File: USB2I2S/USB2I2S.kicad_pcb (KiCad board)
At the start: 2 copper layers, 27.9 x 38.1 mm, 12 parts, among them J1 Conn_01x08_Male, J2 Conn_01x04_Male, J3 Conn_01x02_Male, J5 Conn_01x01_Male, J8 USB_B_Micro, J9 Conn_01x06_Male, U6 CP2615-A01-GM

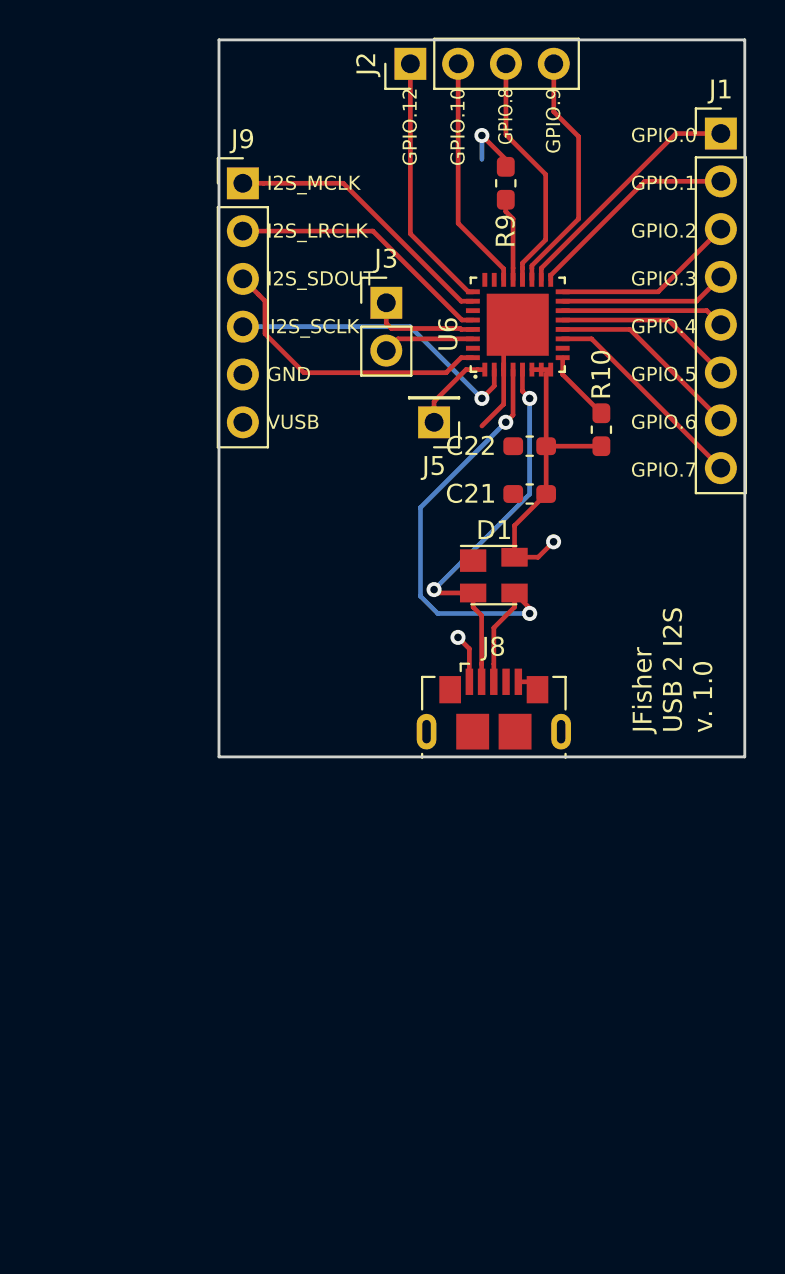
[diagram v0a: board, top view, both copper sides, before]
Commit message: Update USB2I2S board to fix routing issue
- Fixed issue where VCC was connected to VUSB
- Converted PCB to 4-layer board with Vcc and GND planes
- Removed headers for pins that I'm not expecting to use
- Re-layed out the PCB.
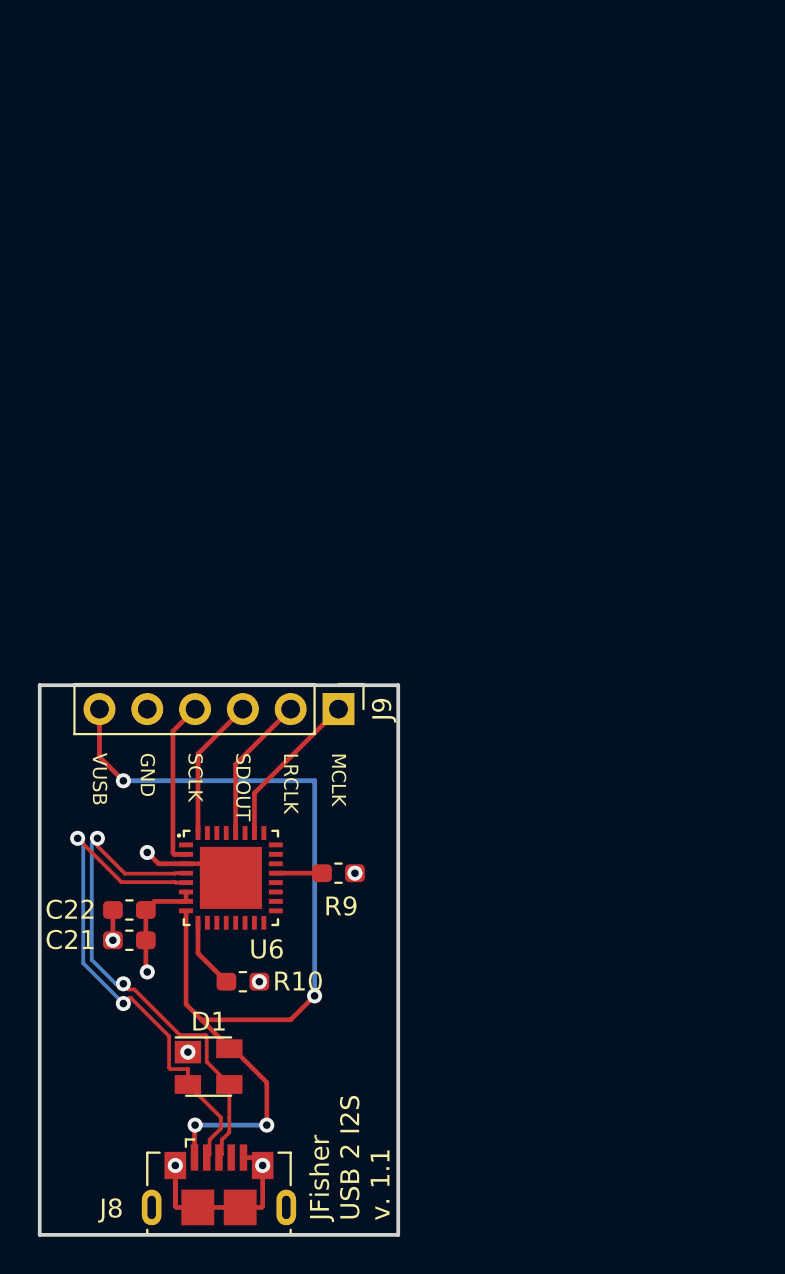
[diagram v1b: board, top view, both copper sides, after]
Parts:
- removed J1: Conn_01x08_Male, Connector_PinHeader_2.54mm:PinHeader_1x08_P2.54mm_Vertical
- removed J2: Conn_01x04_Male, Connector_PinHeader_2.54mm:PinHeader_1x04_P2.54mm_Vertical
- removed J3: Conn_01x02_Male, Connector_PinHeader_2.54mm:PinHeader_1x02_P2.54mm_Vertical
- removed J5: Conn_01x01_Male, Connector_PinHeader_2.54mm:PinHeader_1x01_P2.54mm_Vertical
- moved R9 37.7 mm to (119.4, 121.8), turned to 180 degrees
- moved R10 35.0 mm to (114.3, 127.5), turned to 180 degrees
- moved U6 33.1 mm to (113.7, 122.0), turned to 0 degrees
- moved C22 32.6 mm to (108.3, 123.7)
- moved C21 31.9 mm to (108.3, 125.3)
- moved D1 30.2 mm to (112.5, 132.0)
- moved J8 29.2 mm to (113.0, 138.3)
- moved J9 28.4 mm to (119.4, 113.0), turned to 270 degrees
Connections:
- net VBUS_DN renamed USB_DN
- net VBUS_DP renamed USB_DP
- C21 pad 1: VBUS_IN -> VCC
- C22 pad 1: VBUS_IN -> VCC
- R10 pad 1: VBUS_IN -> VCC
- R9 pad 1: VBUS_IN -> VCC
- U6 pad 1: Net-(J5-Pad1) -> (no net)
- U6 pad 11: Net-(J1-Pad8) -> (no net)
- U6 pad 12: Net-(J1-Pad7) -> (no net)
- U6 pad 13: Net-(J1-Pad6) -> (no net)
- U6 pad 14: Net-(J1-Pad5) -> (no net)
- U6 pad 15: Net-(J1-Pad4) -> (no net)
- U6 pad 16: Net-(J1-Pad3) -> (no net)
- U6 pad 17: Net-(J1-Pad2) -> (no net)
- U6 pad 18: Net-(J1-Pad1) -> (no net)
- U6 pad 19: Net-(J2-Pad4) -> (no net)
- U6 pad 20: Net-(J2-Pad3) -> (no net)
- U6 pad 22: Net-(J2-Pad2) -> (no net)
- U6 pad 25: Net-(J2-Pad1) -> (no net)
- U6 pad 29: Net-(J3-Pad1) -> (no net)
- U6 pad 30: Net-(J3-Pad2) -> (no net)
- U6 pad 6: VBUS_IN -> VCC
- U6 pad 7: VBUS_IN -> VCC
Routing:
- net VBUS_IN: track 23.2 -> 51.3 mm, vias 3 -> 4
- net Net-(J2-Pad1): track 13.6 -> 0.00 mm
- net Net-(J1-Pad1): track 13.1 -> 0.00 mm
- net Net-(J2-Pad4): track 13.1 -> 0.00 mm
- net Net-(J2-Pad3): track 12.9 -> 0.00 mm
- net Net-(J2-Pad2): track 12.5 -> 0.00 mm
- net GND: track 7.36 -> 19.0 mm, vias 0 -> 5
- net Net-(J1-Pad2): track 11.4 -> 0.00 mm
- net Net-(J1-Pad8): track 11.3 -> 0.00 mm
- net Net-(J1-Pad7): track 10.4 -> 0.00 mm
- net Net-(J1-Pad3): track 9.79 -> 0.00 mm
- net Net-(J1-Pad6): track 9.56 -> 0.00 mm
- net Net-(J1-Pad4): track 8.94 -> 0.00 mm
- net Net-(J1-Pad5): track 8.72 -> 0.00 mm
- net I2S_SDOUT: track 15.6 -> 7.57 mm
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- added copper zone on In1.Cu, net GND
- added copper zone on In2.Cu, net VCC
- removed copper zone on F.Cu, net GND
- removed copper zone on B.Cu, net VBUS_IN
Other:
- board size 27.9 x 38.1 mm -> 19.1 x 29.2 mm
- copper layers 2 -> 4
- board text added: "JFisher USB 2 I2S v. 1.1"
- board text added: "LRCLK"
- board text added: "MCLK"
- board text added: "SCLK"
- board text added: "SDOUT"
- board text removed: "GPIO.0"
- board text removed: "GPIO.1"
- board text removed: "GPIO.10"
- board text removed: "GPIO.12"
- board text removed: "GPIO.2"
- board text removed: "GPIO.3"
- board text removed: "GPIO.4"
- board text removed: "GPIO.5"
- board text removed: "GPIO.6"
- board text removed: "GPIO.7"
- board text removed: "GPIO.8"
- board text removed: "GPIO.9"
- board text removed: "I2S_LRCLK"
- board text removed: "I2S_MCLK"
- board text removed: "I2S_SCLK"
- board text removed: "I2S_SDOUT"
- board text removed: "JFisher USB 2 I2S v. 1.0"

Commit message: Update KiCad and minor adjustments (cosmetic)
Rotated the decoupling caps on Vcc to ensure that the blind vias were
away from the differential USB signal traces.
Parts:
- moved C21 1.77 mm to (109.6, 124.1), turned to 270 degrees
- moved C22 0.54 mm to (108.0, 124.1), turned to 270 degrees
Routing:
- net VCC: track 6.15 -> 3.84 mm, vias 3 -> 4
- net GND: vias 5 -> 6
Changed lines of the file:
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@@
-(kicad_pcb (version 20171130) (host pcbnew "(5.0.2)-1")
+(kicad_pcb (version 20171130) (host pcbnew "(5.1.0)-1")
   (general
     (thickness 1.6)
     (drawings 11)
-    (tracks 108)
+    (tracks 110)
     (zones 0)
     (modules 8)
@@
     (0 F.Cu signal)
     (1 In1.Cu signal)
-    (2 In2.Cu signal hide)
+    (2 In2.Cu signal)
     (31 B.Cu signal)
     (33 F.Adhes user)
@@
     (zone_45_only no)
     (trace_min 0.2)
-    (segment_width 0.2)
-    (edge_width 0.15)
     (via_size 0.8)
     (via_drill 0.4)
@@
     (uvia_min_size 0.2)
     (uvia_min_drill 0.1)
+    (edge_width 0.15)
+    (segment_width 0.2)
     (pcb_text_width 0.3)
     (pcb_text_size 1.5 1.5)
@@
   )
   (module Capacitor_SMD:C_0603_1608Metric_Pad1.05x0.95mm_HandSolder (layer F.Cu)
-    (at 108.268472 125.313627 180)
+    (at 109.601 124.141528 270)
     (descr "Capacitor SMD 0603 (1608 Metric), square (rectangular) end terminal, IPC_7351 nominal with elongated pad for handsoldering. (Body size source: http://www.tortai-tech.com/upload/download/2011102023233369053.pdf), generated with kicad-footprint-generator")
     (tags "capacitor handsolder")
     (attr smd)
-    (fp_text reference C21 (at 3.124999 0 180) (layer F.SilkS)
-      (effects (font (size 1 1) (thickness 0.15)))
-    )
-    (fp_text value 1uF (at 0 0 180) (layer F.Fab)
-      (effects (font (size 1 1) (thickness 0.15)))
-    )
-    (fp_text user %R (at 0 0 180) (layer F.Fab)
+    (fp_text reference C21 (at 3.124999 0 270) (layer F.SilkS)
+      (effects (font (size 1 1) (thickness 0.15)))
+    )
+    (fp_text value 1uF (at 0 0 270) (layer F.Fab)
+      (effects (font (size 1 1) (thickness 0.15)))
+    )
+    (fp_text user %R (at 0 0 270) (layer F.Fab)
       (effects (font (size 0.4 0.4) (thickness 0.06)))
     )
@@
     (fp_line (start -0.8 -0.4) (end 0.8 -0.4) (layer F.Fab) (width 0.1))
     (fp_line (start -0.8 0.4) (end -0.8 -0.4) (layer F.Fab) (width 0.1))
-    (pad 2 smd roundrect (at 0.875 0 180) (size 1.05 0.95) (layers F.Cu F.Paste F.Mask) (roundrect_rratio 0.25)
-      (net 1 GND))
-    (pad 1 smd roundrect (at -0.875 0 180) (size 1.05 0.95) (layers F.Cu F.Paste F.Mask) (roundrect_rratio 0.25)
+    (pad 2 smd roundrect (at 0.875 0 270) (size 1.05 0.95) (layers F.Cu F.Paste F.Mask) (roundrect_rratio 0.25)
+      (net 1 GND))
+    (pad 1 smd roundrect (at -0.875 0 270) (size 1.05 0.95) (layers F.Cu F.Paste F.Mask) (roundrect_rratio 0.25)
       (net 9 VCC))
     (model ${KISYS3DMOD}/Capacitor_SMD.3dshapes/C_0603_1608Metric.wrl
@@
   )
   (module Capacitor_SMD:C_0603_1608Metric_Pad1.05x0.95mm_HandSolder (layer F.Cu)
-    (at 108.268472 123.7065 180)
+    (at 107.95 124.141528 270)
     (descr "Capacitor SMD 0603 (1608 Metric), square (rectangular) end terminal, IPC_7351 nominal with elongated pad for handsoldering. (Body size source: http://www.tortai-tech.com/upload/download/2011102023233369053.pdf), generated with kicad-footprint-generator")
     (tags "capacitor handsolder")
     (attr smd)
-    (fp_text reference C22 (at 3.124999 0 180) (layer F.SilkS)
-      (effects (font (size 1 1) (thickness 0.15)))
-    )
-    (fp_text value 0.1uF (at 0 0 180) (layer F.Fab)
+    (fp_text reference C22 (at 3.124999 0 270) (layer F.SilkS)
+      (effects (font (size 1 1) (thickness 0.15)))
+    )
+    (fp_text value 0.1uF (at 0 0 270) (layer F.Fab)
       (effects (font (size 1 1) (thickness 0.15)))
     )
@@
     (fp_line (start 1.65 -0.73) (end 1.65 0.73) (layer F.CrtYd) (width 0.05))
     (fp_line (start 1.65 0.73) (end -1.65 0.73) (layer F.CrtYd) (width 0.05))
-    (fp_text user %R (at 0 0 180) (layer F.Fab)
+    (fp_text user %R (at 0 0 270) (layer F.Fab)
       (effects (font (size 0.4 0.4) (thickness 0.06)))
     )
-    (pad 1 smd roundrect (at -0.875 0 180) (size 1.05 0.95) (layers F.Cu F.Paste F.Mask) (roundrect_rratio 0.25)
+    (pad 1 smd roundrect (at -0.875 0 270) (size 1.05 0.95) (layers F.Cu F.Paste F.Mask) (roundrect_rratio 0.25)
       (net 9 VCC))
-    (pad 2 smd roundrect (at 0.875 0 180) (size 1.05 0.95) (layers F.Cu F.Paste F.Mask) (roundrect_rratio 0.25)
+    (pad 2 smd roundrect (at 0.875 0 270) (size 1.05 0.95) (layers F.Cu F.Paste F.Mask) (roundrect_rratio 0.25)
       (net 1 GND))
     (model ${KISYS3DMOD}/Capacitor_SMD.3dshapes/C_0603_1608Metric.wrl
@@
   (segment (start 111.28 121.25) (end 109.82 121.25) (width 0.25) (layer F.Cu) (net 1))
   (segment (start 109.82 121.25) (end 109.22 120.65) (width 0.25) (layer F.Cu) (net 1))
-  (segment (start 107.393472 123.7065) (end 107.393472 125.313627) (width 0.25) (layer F.Cu) (net 1))
-  (via (at 107.393472 125.313627) (size 0.8) (drill 0.4) (layers F.Cu B.Cu) (net 1))
-  (via (at 111.379 131.2575) (size 0.8) (drill 0.4) (layers F.Cu B.Cu) (net 1))
+  (via blind (at 111.379 131.2575) (size 0.8) (drill 0.4) (layers F.Cu In1.Cu) (net 1))
   (segment (start 114.93 136.8615) (end 115.35 137.2815) (width 0.25) (layer F.Cu) (net 1))
   (segment (start 114.33 136.8615) (end 114.93 136.8615) (width 0.25) (layer F.Cu) (net 1))
@@
   (segment (start 110.78 139.5115) (end 110.71 139.4415) (width 0.25) (layer F.Cu) (net 1))
   (segment (start 111.905 139.5115) (end 110.78 139.5115) (width 0.25) (layer F.Cu) (net 1))
-  (via (at 110.71 137.2815) (size 0.8) (drill 0.4) (layers F.Cu B.Cu) (net 1))
+  (via blind (at 110.71 137.2815) (size 0.8) (drill 0.4) (layers F.Cu In1.Cu) (net 1))
   (segment (start 110.71 137.2815) (end 110.71 139.4415) (width 0.25) (layer F.Cu) (net 1))
-  (via (at 115.35 137.2815) (size 0.8) (drill 0.4) (layers F.Cu B.Cu) (net 1))
+  (via blind (at 115.35 137.2815) (size 0.8) (drill 0.4) (layers F.Cu In1.Cu) (net 1))
+  (segment (start 109.601 125.016528) (end 109.601 125.016528) (width 0.25) (layer F.Cu) (net 1))
+  (segment (start 107.95 125.016528) (end 107.95 125.016528) (width 0.25) (layer F.Cu) (net 1))
+  (via blind (at 107.95 125.016528) (size 0.8) (drill 0.4) (layers F.Cu In1.Cu) (net 1))
+  (segment (start 109.601 125.016528) (end 107.95 125.016528) (width 0.25) (layer F.Cu) (net 1))
+  (via blind (at 109.601 125.016528) (size 0.8) (drill 0.4) (layers F.Cu In1.Cu) (net 1))
   (segment (start 111.73 136.8615) (end 111.73 135.1665) (width 0.25) (layer F.Cu) (net 2))
   (segment (start 111.73 135.1665) (end 111.76 135.1365) (width 0.25) (layer F.Cu) (net 2))
@@
   (segment (start 113.425 127.5165) (end 111.915 126.0065) (width 0.25) (layer F.Cu) (net 8))
   (via blind (at 120.255 121.75) (size 0.8) (drill 0.4) (layers F.Cu In2.Cu) (net 9))
-  (segment (start 109.143472 125.313627) (end 109.143472 123.7065) (width 0.25) (layer F.Cu) (net 9))
-  (segment (start 109.599972 123.25) (end 111.28 123.25) (width 0.25) (layer F.Cu) (net 9))
-  (segment (start 109.143472 123.7065) (end 109.599972 123.25) (width 0.25) (layer F.Cu) (net 9))
   (segment (start 111.28 122.75) (end 111.28 123.25) (width 0.25) (layer F.Cu) (net 9))
-  (via blind (at 109.22 127) (size 0.8) (drill 0.4) (layers F.Cu In2.Cu) (net 9))
-  (segment (start 109.143472 125.313627) (end 109.143472 126.923472) (width 0.25) (layer F.Cu) (net 9))
-  (segment (start 109.143472 126.923472) (end 109.22 127) (width 0.25) (layer F.Cu) (net 9))
   (via blind (at 115.175 127.5165) (size 0.8) (drill 0.4) (layers F.Cu In2.Cu) (net 9))
+  (segment (start 107.95 123.266528) (end 109.601 123.266528) (width 0.25) (layer F.Cu) (net 9))
+  (segment (start 109.617528 123.25) (end 109.601 123.266528) (width 0.25) (layer F.Cu) (net 9))
+  (segment (start 111.28 123.25) (end 109.617528 123.25) (width 0.25) (layer F.Cu) (net 9))
+  (via blind (at 109.601 123.266528) (size 0.8) (drill 0.4) (layers F.Cu In2.Cu) (net 9))
+  (via blind (at 107.95 123.266528) (size 0.8) (drill 0.4) (layers F.Cu In2.Cu) (net 9))
   (segment (start 112.529999 136.711501) (end 112.529999 135.921499) (width 0.2) (layer F.Cu) (net 10))
   (segment (start 112.38 136.8615) (end 112.529999 136.711501) (width 0.2) (layer F.Cu) (net 10))

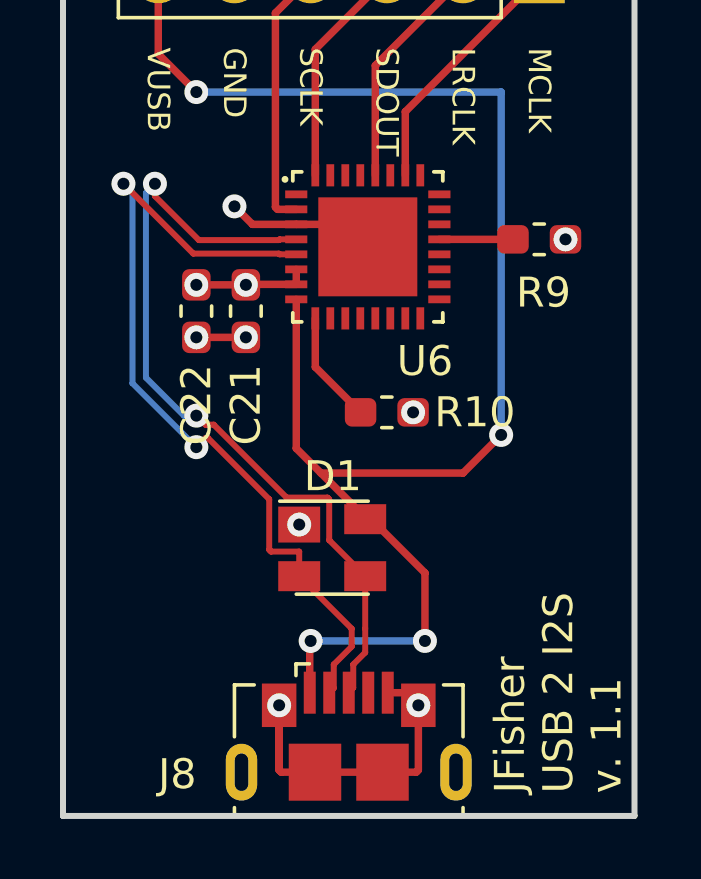
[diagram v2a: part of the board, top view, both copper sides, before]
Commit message: Convert blind vias to through vias
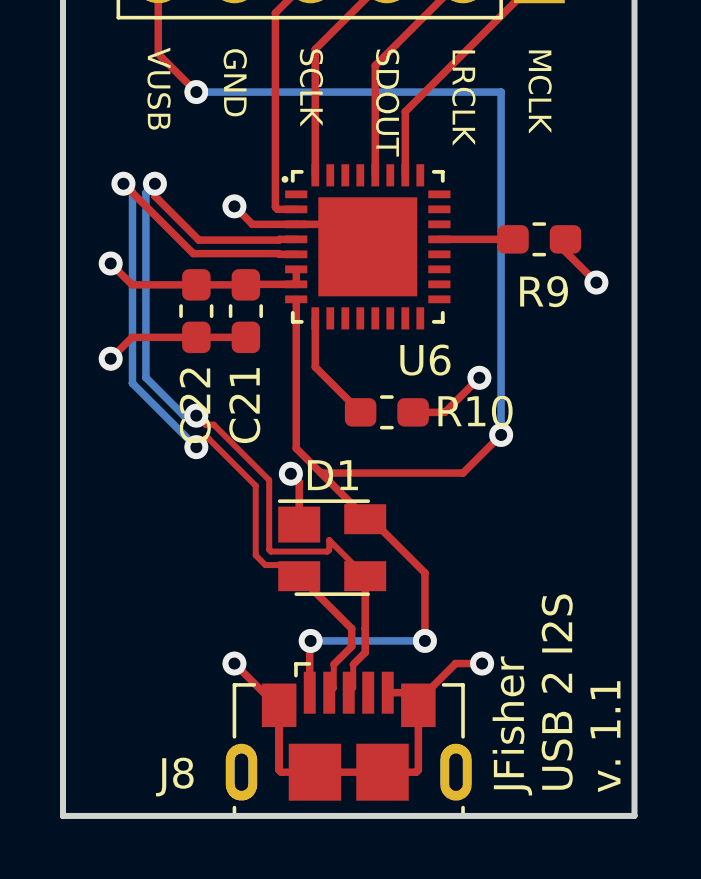
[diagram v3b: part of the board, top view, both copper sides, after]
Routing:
- net GND: track 19.0 -> 28.8 mm, vias 6 -> 5
- net VCC: track 3.84 -> 11.5 mm, vias 4 -> 3
- net USB_DP: track 27.3 -> 28.4 mm
